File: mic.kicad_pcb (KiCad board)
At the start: 2 copper layers, 50 x 50 mm, 38 parts, among them J1 AudioPlug3, J2 USB_C_Receptacle_USB2.0_16P, SW1 SW_Push, U1 TS5A3159ADBVR, U2 INA826AID, U3 PCM2902CDBR, U4 TLV70033_SOT23-5, Y1 12MHz

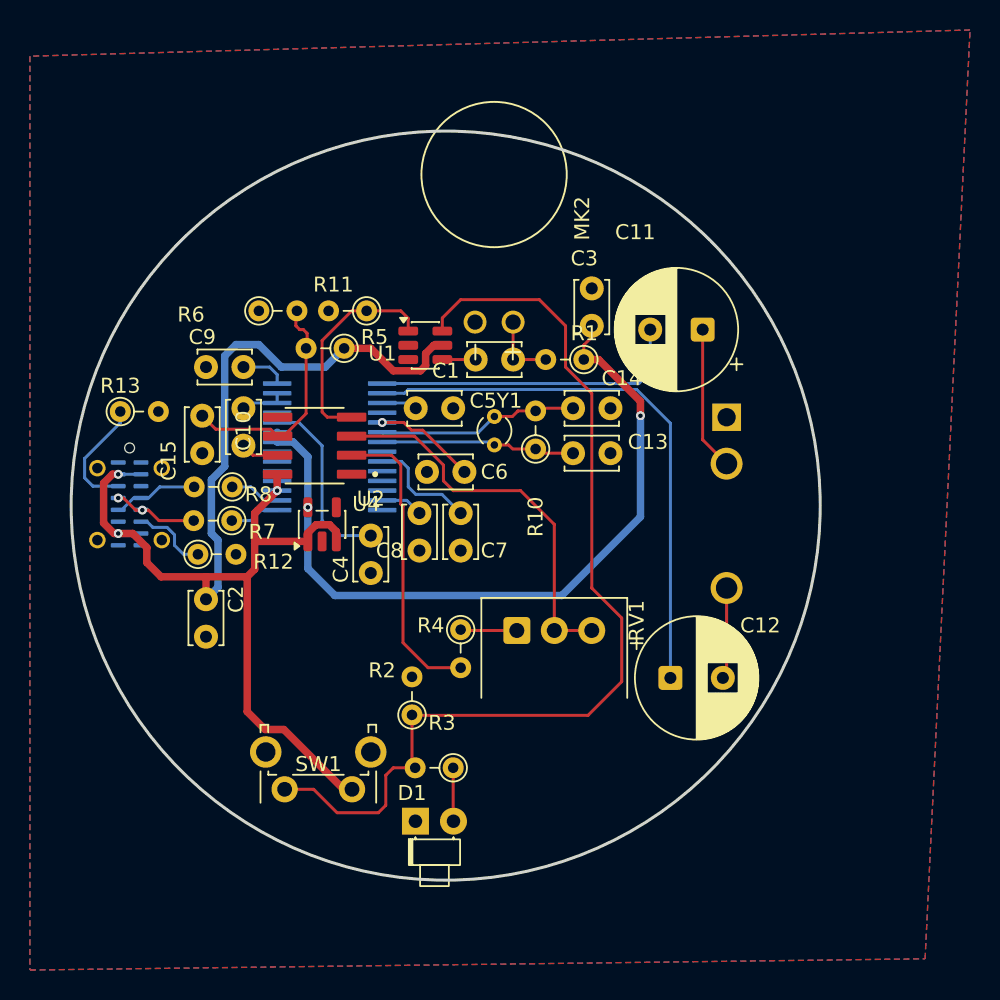
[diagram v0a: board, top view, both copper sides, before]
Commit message: Add mic-bias/VBUS filters, codec input R, USB ESD; stereo jack
- R14/C18 mic-bias RC filter, R15 codec input resistor
- R16/C19 VBUS filter for PCM2902C, U5 USBLC6-2SC6 on D+/D-
- J1 -> PJ-3920-3A stereo jack (custom footprint in mic.pretty)
- All passives THT; C3 moved next to LDO; reroutes under U3
- LCSC: J2 C2843970, U3 code removed; R3 1k
- review.md updated

Co-Authored-By: Claude Opus 5.5 <noreply@anthropic.com>
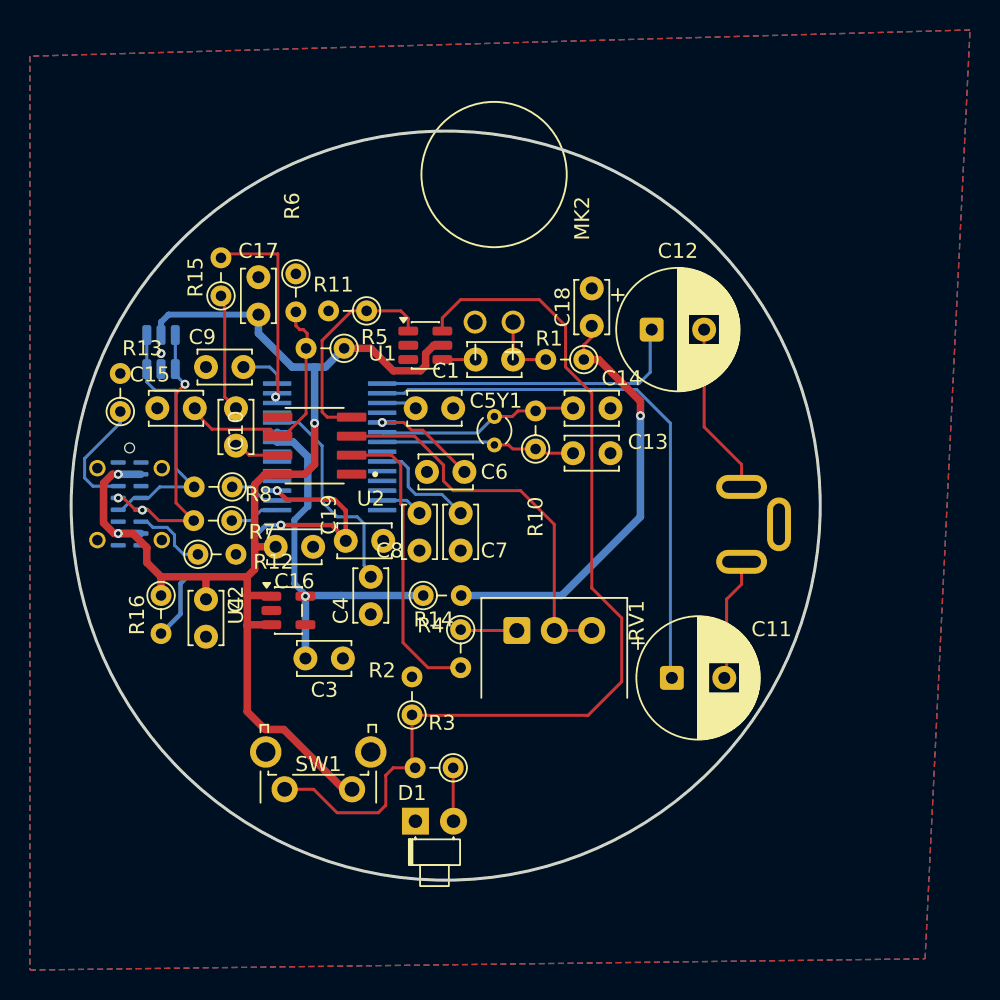
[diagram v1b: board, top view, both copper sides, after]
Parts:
- added C16: 100n, Capacitor_THT:C_Disc_D3.4mm_W2.1mm_P2.50mm, F.Cu at (91.2, 102.8)
- added C17: 100n, Capacitor_THT:C_Disc_D3.4mm_W2.1mm_P2.50mm, F.Cu at (87.5, 84.8)
- added C18: 10u, Capacitor_THT:C_Disc_D3.4mm_W2.1mm_P2.50mm, F.Cu at (109.8, 88.0)
- added C19: 1u, Capacitor_THT:C_Disc_D3.4mm_W2.1mm_P2.50mm, F.Cu at (93.3, 102.3)
- added R14: 1k, Resistor_THT:R_Axial_DIN0204_L3.6mm_D1.6mm_P2.54mm_Vertical, F.Cu at (98.5, 106.0)
- added R15: 1k, Resistor_THT:R_Axial_DIN0204_L3.6mm_D1.6mm_P2.54mm_Vertical, F.Cu at (85.0, 86.0)
- added R16: 2R2, Resistor_THT:R_Axial_DIN0204_L3.6mm_D1.6mm_P2.54mm_Vertical, F.Cu at (81.0, 106.0)
- added U5: USBLC6-2SC6, Package_TO_SOT_SMD:SOT-23-6, B.Cu at (81.0, 89.8)
- J1: footprint Connector_Audio:Jack_3.5mm_QingPu_WQP-PJ398SM_Vertical_CircularHoles -> mic:Jack_3.5mm_KoreanHropartsElec_PJ-3920-3A_Vertical
- R1: value 2k2 -> 1k2
- R3: value 150R -> 1kR
- moved C3 29.3 mm to (90.6, 110.2), turned to 0 degrees
- moved C11 23.3 mm to (115.1, 111.5), turned to 0 degrees
- moved C12 23.3 mm to (113.8, 88.2)
- moved J1 7.22 mm to (119.8, 101.2), turned to 90 degrees
- moved U4 6.17 mm to (89.5, 107.0), turned to 0 degrees
- moved C15 4.24 mm to (80.8, 93.5), turned to 0 degrees
- moved R6 3.49 mm to (90.0, 84.5), turned to -90 degrees
- moved C4 2.75 mm to (95.0, 107.2)
- moved C10 0.50 mm to (86.0, 93.5)
- turned R13 to 90 degrees
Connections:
- net Net-(J2-D+-PadA6) renamed /USB_DP
- net Net-(J2-D--PadA7) renamed /USB_DM
- C10 pad 1: Net-(U3-VINL) -> Net-(C10-Pad1)
- C11 pad 1: Net-(C11-Pad1) -> Net-(U3-VOUTL)
- C11 pad 2: Net-(U3-VOUTR) -> Net-(C11-Pad2)
- C12 pad 1: Net-(U3-VOUTL) -> Net-(U3-VOUTR)
- J1 pad R: Net-(C11-Pad1) -> Net-(C12-Pad2)
- J1 pad T: Net-(C12-Pad2) -> Net-(C11-Pad2)
- R1 pad 1: +3.3V -> /MIC_BIAS
- U1 pad 3: unconnected-(U1-Pad3) -> Earth
- U3 pad 3: +5V -> Net-(U3-VBUS)
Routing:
- net /MIC_BIAS: track 0.00 -> 29.2 mm, vias 0 -> 1
- net +3.3V: track 50.8 -> 25.1 mm, vias 2 -> 1
- net Net-(U3-VBUS): track 0.00 -> 25.5 mm, vias 0 -> 2
- net /USB_DP: track 5.67 -> 18.7 mm, vias 2 -> 3
- net /USB_DM: track 5.70 -> 18.0 mm
- net Net-(U3-VINL): track 3.04 -> 14.4 mm, vias 0 -> 1
- net Net-(C11-Pad1): track 10.1 -> 0.00 mm
- net Net-(C11-Pad2): track 0.00 -> 8.32 mm
- net Net-(C10-Pad1): track 0.00 -> 7.85 mm
- net Net-(C12-Pad2): track 6.10 -> 11.5 mm
- net Net-(U3-VCCCI): track 12.3 -> 14.5 mm
- net +5V: track 88.0 -> 86.0 mm
- net Net-(U2-REF): track 15.5 -> 16.2 mm
- net Earth: vias 0 -> 1
